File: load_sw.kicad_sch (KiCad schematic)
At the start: 49 parts, among them Q1 PSMN020-100YS, Q11 NMOS, Q16 NMOS, Q21 NMOS, Q22 NPN, Q23 NMOS, Q36 Q_NMOS, Q37 NPN, Q38 NMOS, Q6 NPN, U4 TPS16851VMAR, U5 LM5050-1

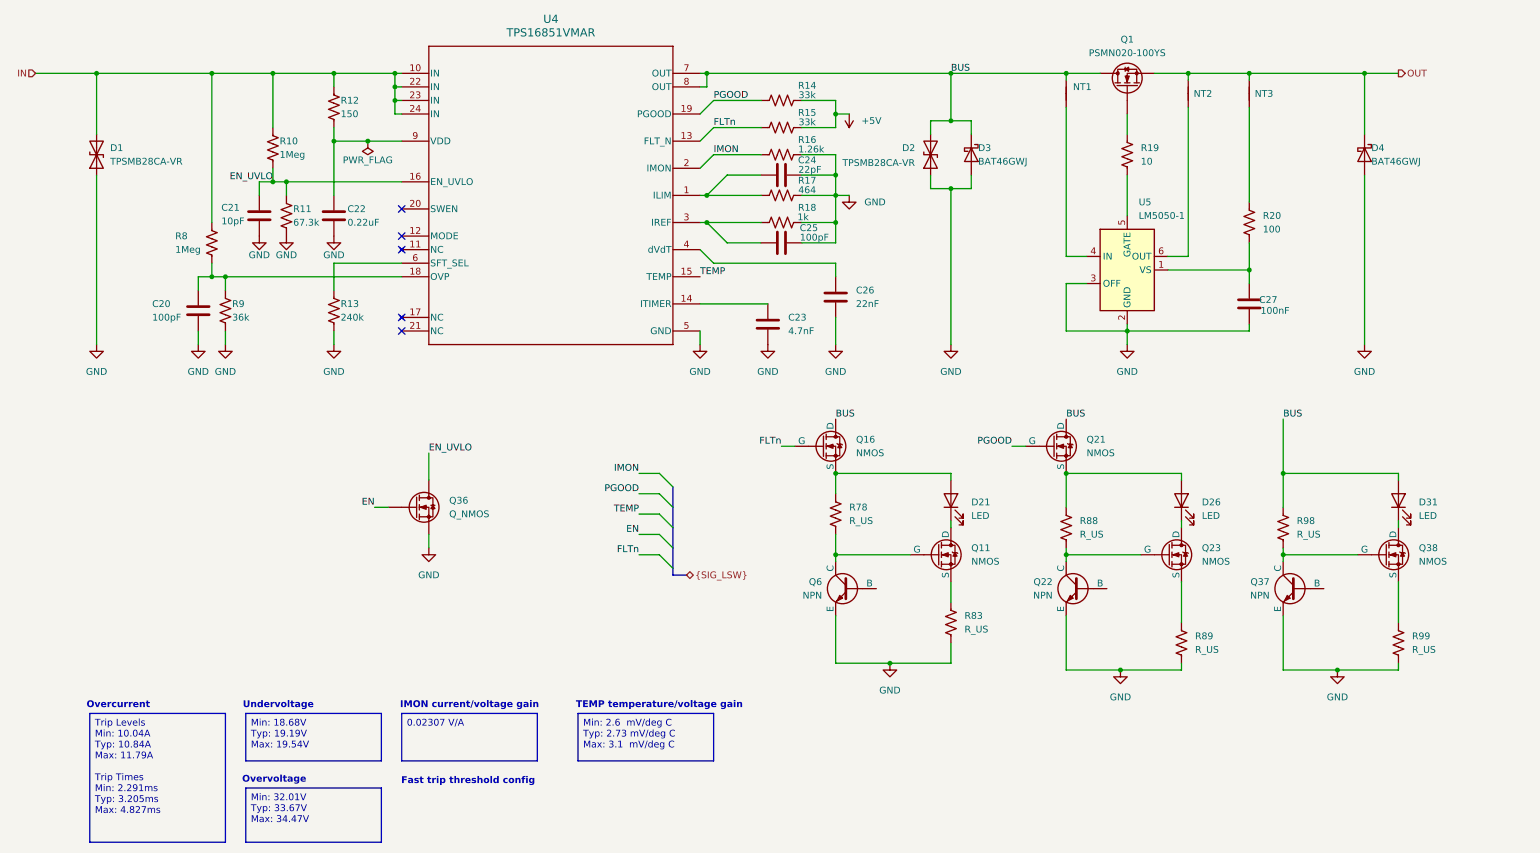
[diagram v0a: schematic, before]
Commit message: Finished layout for load switch dev board.
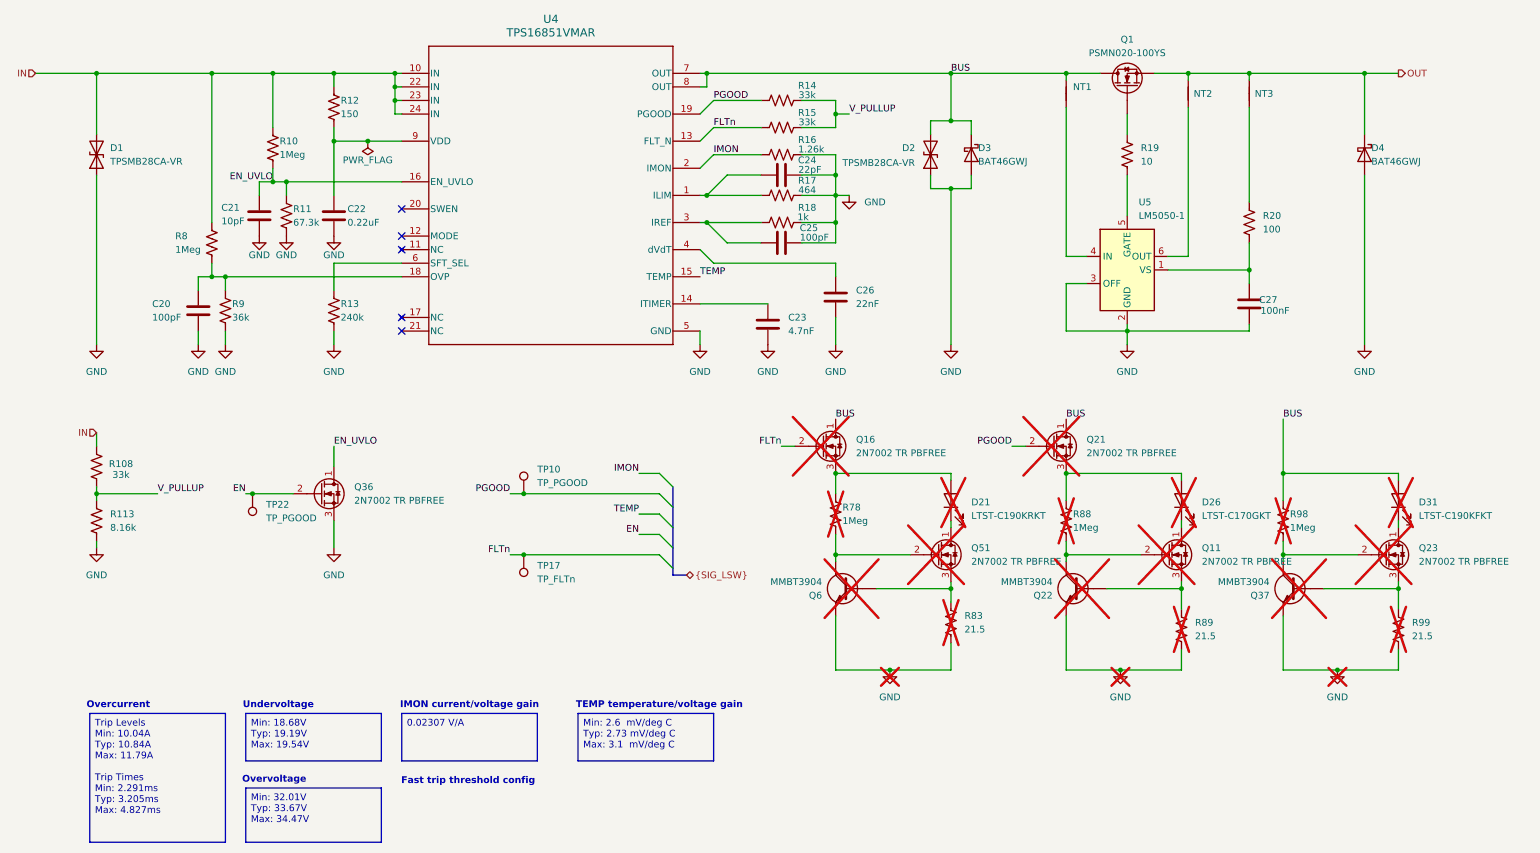
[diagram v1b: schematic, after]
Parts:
- removed Q11, Q16, Q21, Q23, Q38: NMOS, symbol Simulation_SPICE:NMOS
- removed Q22, Q37, Q6: NPN, symbol Simulation_SPICE:NPN
- removed Q36: Q_NMOS, symbol Device:Q_NMOS
- added Q11, Q16, Q21, Q23, Q36, Q51: 2N7002 TR PBFREE, Package_TO_SOT_SMD:TSOT-23, symbol Transistor_FET:Q_NMOS_DGS
- added Q22, Q37, Q6: MMBT3904, Package_TO_SOT_SMD:TSOT-23, symbol Device:Q_NPN
- added R108: 33k, Resistor_SMD:R_0603_1608Metric, symbol Device:R_US
- added R113: 8.16k, Resistor_SMD:R_0603_1608Metric, symbol Device:R_US
- added TP10, TP22: TP_PGOOD, TestPoint:TestPoint_Plated_Hole_D5.0mm, symbol Connector:TestPoint
- added TP17: TP_FLTn, TestPoint:TestPoint_Plated_Hole_D5.0mm, symbol Connector:TestPoint
- D21: value LED -> LTST-C190KRKT; footprint (none) -> LED_SMD:LED_0603_1608Metric; Mfr (none) -> Lite-On Inc.; Mfr P/N (none) -> LTST-C190KRKT; Supplier_1 (none) -> Digikey; Supplier_1 P/N (none) -> 160-1436-2-ND; Supplier_1 Price @ Qty (none) -> 1; Supplier_1 Unit Price (none) -> 0.14000; now not fitted; now left out of the parts list
- D26: value LED -> LTST-C170GKT; footprint (none) -> LED_SMD:LED_0805_2012Metric; Mfr (none) -> Lite-On Inc.; Mfr P/N (none) -> LTST-C170GKT; Supplier_1 (none) -> Digikey; Supplier_1 P/N (none) -> 160-1179-2-ND; Supplier_1 Price @ Qty (none) -> 1; Supplier_1 Unit Price (none) -> 0.10000; now not fitted; now left out of the parts list
- D31: value LED -> LTST-C190KFKT; footprint (none) -> LED_SMD:LED_0603_1608Metric; Mfr (none) -> Lite-On Inc.; Mfr P/N (none) -> LTST-C190KFKT; Supplier_1 (none) -> Digikey; Supplier_1 P/N (none) -> 160-1434-2-ND; Supplier_1 Price @ Qty (none) -> 1; Supplier_1 Unit Price (none) -> 0.13000; now not fitted; now left out of the parts list
- R78, R88, R98: value R_US -> 1Meg; footprint (none) -> Resistor_SMD:R_0603_1608Metric; Mfr (none) -> Stackpole Electronics Inc; Mfr P/N (none) -> RNCF0603BKC1M00; Supplier_1 (none) -> Digikey; Supplier_1 P/N (none) -> RNCF0603BKC1M00TR-ND; Supplier_1 Price @ Qty (none) -> 1; Supplier_1 Unit Price (none) -> 0.11000; now not fitted; now left out of the parts list
- R83, R89, R99: value R_US -> 21.5; footprint (none) -> Resistor_SMD:R_0603_1608Metric; Mfr (none) -> KOA Speer Electronics, Inc.; Mfr P/N (none) -> RN73R1JTTD21R5B25; Supplier_1 (none) -> Digikey; Supplier_1 P/N (none) -> 2019-RN73R1JTTD21R5B25TR-ND; Supplier_1 Price @ Qty (none) -> 0.12000; Supplier_1 Unit Price (none) -> 1; now not fitted; now left out of the parts list
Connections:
- net BUS: now also Q16.1 (D), Q21.1 (D)
- net EN: now also Q36.2 (G), TP22.1
- net EN_UVLO: now also Q36.1 (D)
- net FLTn: now also Q16.2 (G), TP17.1
- net GND: now also Q22.E, Q36.3 (S), Q37.E, Q6.E, R113.2
- net IN: now also R108.2
- net PGOOD: now also Q21.2 (G), TP10.1
- net at D31.1 (K): now also Q23.1 (D)
- net at R98.2: now also Q23.2 (G), Q37.C
- net at R99.1: now also Q23.3 (S), Q37.B
- net at R83.1: now also Q51.3 (S), Q6.B
- net at R88.2: now also Q11.2 (G), Q22.C
- net at D26.2 (A), R88.1: now also Q21.3 (S)
- net at R89.1: now also Q11.3 (S), Q22.B
- net at D21.2 (A), R78.1: now also Q16.3 (S)
- net at D21.1 (K): now also Q51.1 (D)
- net at R78.2: now also Q51.2 (G), Q6.C
- net at D26.1 (K): now also Q11.1 (D)
- net +5V renamed V_PULLUP
- net V_PULLUP: now also R108.1, R113.1

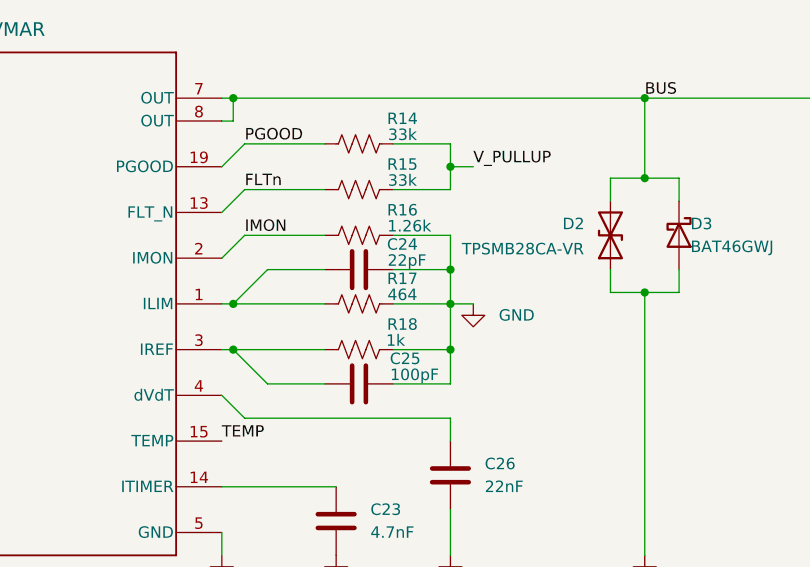
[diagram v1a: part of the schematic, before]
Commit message: Removing pads and adding more TPs and also mounting holes
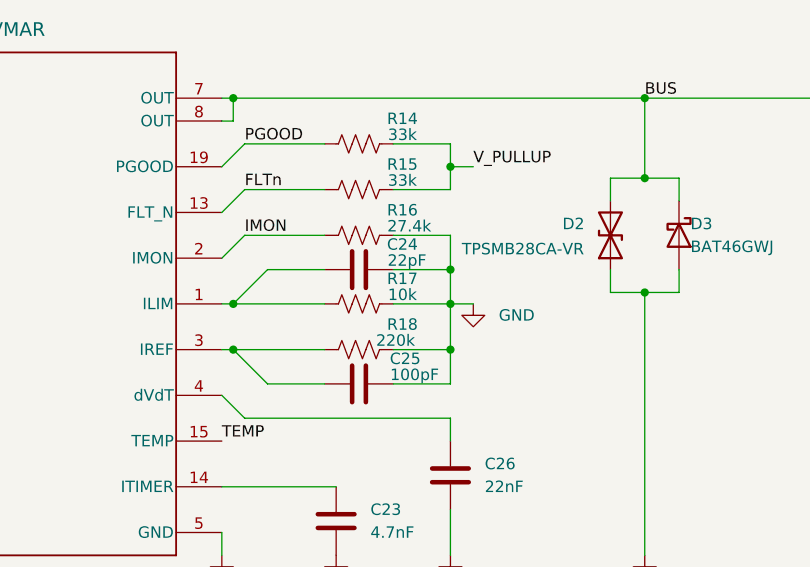
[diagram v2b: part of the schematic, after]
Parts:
- R16: value 1.26k -> 27.4k; Mfr KOA Speer Electronics, Inc. -> Panasonic Electronic Components; Mfr P/N RN73R1JTTD1261B25 -> ERA-3AEB2742V; Supplier_1 P/N 2019-RN73R1JTTD1261B25TR-ND -> P27.4KDBTR-ND; Supplier_1 Unit Price 0.12000 -> 0.10000
- R17: value 464 -> 10k; Mfr P/N ERA-3AEB4640V -> ERA-3AEB103V; Supplier_1 P/N 10-ERA-3AEB4640VTR-ND -> P10KDBTR-ND
- R18: value 1k -> 220k; Mfr P/N ERA-3AEB103V -> ERA-3AEB2742V; Supplier_1 P/N P10KDBTR-ND -> P27.4KDBTR-ND
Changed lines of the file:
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@@
 			)
 		)
-		(property "Value" "464"
+		(property "Value" "10k"
 			(at 164.846 53.594 90)
 			(effects
@@
 			)
 		)
-		(property "Description" "RES SMD 464 OHM 0.1% 1/10W 0603"
+		(property "Description" "RES SMD 10K OHM 0.1% 1/10W 0603"
 			(at 160.02 54.61 0)
 			(effects
@@
 			)
 		)
-		(property "Mfr P/N" "ERA-3AEB4640V"
+		(property "Mfr P/N" "ERA-3AEB103V"
 			(at 160.02 54.61 0)
 			(effects
@@
 			)
 		)
-		(property "Supplier_1 P/N" "10-ERA-3AEB4640VTR-ND"
+		(property "Supplier_1 P/N" "P10KDBTR-ND"
 			(at 160.02 54.61 0)
 			(effects
@@
 			)
 		)
-		(property "Value" "1.26k"
+		(property "Value" "27.4k"
 			(at 165.608 45.974 90)
 			(effects
@@
 			)
 		)
-		(property "Datasheet" "https://www.koaspeer.com/pdfs/RN73R.pdf"
+		(property "Datasheet" "https://industrial.panasonic.com/cdbs/www-data/pdf/RDM0000/AOA0000C307.pdf"
 			(at 160.02 46.99 0)
 			(effects
@@
 			)
 		)
-		(property "Description" "RES 1.26K OHM 0.1% 1/10W 0603"
+		(property "Description" "RES SMD 27.4KOHM 0.1% 1/10W 0603"
 			(at 160.02 46.99 0)
 			(effects
@@
 			)
 		)
-		(property "Mfr" "KOA Speer Electronics, Inc."
+		(property "Mfr" "Panasonic Electronic Components"
 			(at 160.02 46.99 0)
 			(effects
@@
 			)
 		)
-		(property "Mfr P/N" "RN73R1JTTD1261B25"
+		(property "Mfr P/N" "ERA-3AEB2742V"
 			(at 160.02 46.99 0)
 			(effects
@@
 			)
 		)
-		(property "Supplier_1 P/N" "2019-RN73R1JTTD1261B25TR-ND"
+		(property "Supplier_1 P/N" "P27.4KDBTR-ND"
 			(at 160.02 46.99 0)
 			(effects
@@
 			)
 		)
-		(property "Supplier_1 Unit Price" "0.12000"
+		(property "Supplier_1 Unit Price" "0.10000"
 			(at 160.02 46.99 0)
 			(effects
@@
 			)
 		)
-		(property "Value" "1k"
+		(property "Value" "220k"
 			(at 164.084 58.674 90)
 			(effects
@@
 			)
 		)
-		(property "Description" "RES SMD 10K OHM 0.1% 1/10W 0603"
+		(property "Description" "RES SMD 27.4KOHM 0.1% 1/10W 0603"
 			(at 160.02 59.69 0)
 			(effects
@@
 			)
 		)
-		(property "Mfr P/N" "ERA-3AEB103V"
+		(property "Mfr P/N" "ERA-3AEB2742V"
 			(at 160.02 59.69 0)
 			(effects
@@
 			)
 		)
-		(property "Supplier_1 P/N" "P10KDBTR-ND"
+		(property "Supplier_1 P/N" "P27.4KDBTR-ND"
 			(at 160.02 59.69 0)
 			(effects

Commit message: Finishing up layout
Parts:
- R16: value 27.4k -> 5.49k; Mfr P/N ERA-3AEB2742V -> ERA-3AEB5491V; Supplier_1 P/N P27.4KDBTR-ND -> P5.49KDBTR-ND
- R17: value 10k -> 2k; Mfr P/N ERA-3AEB103V -> ERA-3AEB202V; Supplier_1 P/N P10KDBTR-ND -> P2.0KDBTR-ND
- R18: value 220k -> 44.8k; Mfr Panasonic Electronic Components -> KOA Speer Electronics, Inc.; Mfr P/N ERA-3AEB2742V -> RN73R1JTTD4482B25; Supplier_1 P/N P27.4KDBTR-ND -> 2019-RN73R1JTTD4482B25TR-ND
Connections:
- net BUS: now also Q1.S; no longer Q1.D
- net OUT: now also Q1.D; no longer Q1.S
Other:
- moved on the sheet: Q1
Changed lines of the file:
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@@
 		)
 	)
-	(text_box "Trip Levels\nMin: 10.04A\nTyp: 10.84A\nMax: 11.79A\n\nTrip Times\nMin: 2.291ms\nTyp: 3.205ms\nMax: 4.827ms"
+	(text_box "Trip Levels\nMin: 10.32A\nTyp: 11.14A\nMax: 12.12A\n\nTrip Times\nMin: 2.291ms\nTyp: 3.205ms\nMax: 4.827ms"
 		(exclude_from_sim no)
 		(at 30.48 151.638 0)
@@
 		)
 	)
-	(text_box "0.02307 V/A"
+	(text_box "0.10052 V/A (nom)"
 		(exclude_from_sim no)
 		(at 88.9 151.638 0)
@@
 			)
 		)
-		(property "Value" "10k"
+		(property "Value" "2k"
 			(at 164.846 53.594 90)
 			(effects
@@
 			)
 		)
-		(property "Description" "RES SMD 10K OHM 0.1% 1/10W 0603"
+		(property "Description" "RES SMD 2K OHM 0.1% 1/10W 0603"
 			(at 160.02 54.61 0)
 			(effects
@@
 			)
 		)
-		(property "Mfr P/N" "ERA-3AEB103V"
+		(property "Mfr P/N" "ERA-3AEB202V"
 			(at 160.02 54.61 0)
 			(effects
@@
 			)
 		)
-		(property "Supplier_1 P/N" "P10KDBTR-ND"
+		(property "Supplier_1 P/N" "P2.0KDBTR-ND"
 			(at 160.02 54.61 0)
 			(effects
@@
 			)
 		)
-		(property "Value" "27.4k"
+		(property "Value" "5.49k"
 			(at 165.608 45.974 90)
 			(effects
@@
 			)
 		)
-		(property "Description" "RES SMD 27.4KOHM 0.1% 1/10W 0603"
+		(property "Description" "RES SMD 5.49KOHM 0.1% 1/10W 0603"
 			(at 160.02 46.99 0)
 			(effects
@@
 			)
 		)
-		(property "Mfr P/N" "ERA-3AEB2742V"
+		(property "Mfr P/N" "ERA-3AEB5491V"
 			(at 160.02 46.99 0)
 			(effects
@@
 			)
 		)
-		(property "Supplier_1 P/N" "P27.4KDBTR-ND"
+		(property "Supplier_1 P/N" "P5.49KDBTR-ND"
 			(at 160.02 46.99 0)
 			(effects
@@
 			)
 		)
-		(property "Value" "220k"
+		(property "Value" "44.8k"
 			(at 164.084 58.674 90)
 			(effects
@@
 			)
 		)
-		(property "Datasheet" "https://industrial.panasonic.com/cdbs/www-data/pdf/RDM0000/AOA0000C307.pdf"
+		(property "Datasheet" "https://www.koaspeer.com/pdfs/RN73R.pdf"
 			(at 160.02 59.69 0)
 			(effects
@@
 			)
 		)
-		(property "Description" "RES SMD 27.4KOHM 0.1% 1/10W 0603"
+		(property "Description" "RES 44.8K OHM 0.1% 1/10W 0603"
 			(at 160.02 59.69 0)
 			(effects
@@
 			)
 		)
-		(property "Mfr" "Panasonic Electronic Components"
+		(property "Mfr" "KOA Speer Electronics, Inc."
 			(at 160.02 59.69 0)
 			(effects
@@
 			)
 		)
-		(property "Mfr P/N" "ERA-3AEB2742V"
+		(property "Mfr P/N" "RN73R1JTTD4482B25"
 			(at 160.02 59.69 0)
 			(effects
@@
 			)
 		)
-		(property "Supplier_1 P/N" "P27.4KDBTR-ND"
+		(property "Supplier_1 P/N" "2019-RN73R1JTTD4482B25TR-ND"
 			(at 160.02 59.69 0)
 			(effects
@@
 	(symbol
 		(lib_id "Device:Q_NMOS")
-		(at 224.79 34.29 90)
+		(at 224.79 34.29 270)
+		(mirror x)
 		(unit 1)
 		(exclude_from_sim no)
@@
 		(on_board yes)
 		(dnp no)
-		(fields_autoplaced yes)
 		(property "Reference" "Q1"
 			(at 224.79 25.4 90)
@@
 		)
 		(property "Footprint" "_Power_Board:LFPAK56_1"
-			(at 222.25 29.21 0)
+			(at 227.33 29.21 0)
 			(effects
 				(font
@@
 			)
 		)
-		(property "Datasheet" "~"
+		(property "Datasheet" "https://my.centralsemi.com/datasheets/2N7002.PDF"
 			(at 73.66 110.49 0)
 			(effects

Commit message: Fixed cap values
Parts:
- C22: Mfr KEMET -> YAGEO; Mfr P/N C0603C221F5GACAUTO -> CC0603JRX7R9BB224; Supplier_1 P/N 399-C0603C221F5GACAUTOTR-ND -> 13-CC0603JRX7R9BB224TR-ND; Supplier_1 Unit Price 0.85000 -> 0.15000
- C23: Mfr P/N GCM1885C2A471FA16D -> GCM1885C1H472FA16D; Supplier_1 P/N 490-GCM1885C2A471FA16DTR-ND -> 490-GCM1885C1H472FA16DTR-ND; Supplier_1 Unit Price 0.16000 -> 0.18000
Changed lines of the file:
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@@
 			)
 		)
-		(property "Datasheet" "https://search.murata.co.jp/Ceramy/image/img/A01X/G101/ENG/GCM1885C2A471FA16-01.pdf"
+		(property "Datasheet" "https://search.murata.co.jp/Ceramy/image/img/A01X/G101/ENG/GCM1885C1H472FA16-01A.pdf"
 			(at 157.48 78.74 0)
 			(effects
@@
 			)
 		)
-		(property "Description" "CAP CER 470PF 100V C0G/NP0 0603"
+		(property "Description" "CAP CER 4700PF 50V C0G/NP0 0603"
 			(at 157.48 78.74 0)
 			(effects
@@
 			)
 		)
-		(property "Mfr P/N" "GCM1885C2A471FA16D"
+		(property "Mfr P/N" "GCM1885C1H472FA16D"
 			(at 157.48 78.74 0)
 			(effects
@@
 			)
 		)
-		(property "Supplier_1 P/N" "490-GCM1885C2A471FA16DTR-ND"
+		(property "Supplier_1 P/N" "490-GCM1885C1H472FA16DTR-ND"
 			(at 157.48 78.74 0)
 			(effects
@@
 			)
 		)
-		(property "Supplier_1 Unit Price" "0.16000"
+		(property "Supplier_1 Unit Price" "0.18000"
 			(at 157.48 78.74 0)
 			(effects
@@
 			)
 		)
-		(property "Datasheet" "https://search.kemet.com/download/datasheet/C0603C221F5GACAUTO"
+		(property "Datasheet" "https://www.yageogroup.com/content/datasheet/asset/file/UPY-GPHC_X7R_6_3V-TO-250V"
 			(at 76.2 58.42 0)
 			(effects
@@
 			)
 		)
-		(property "Description" "CAP CER 220PF 50V C0G/NP0 0603"
+		(property "Description" "CAP CER 0.22UF 50V X7R 0603"
 			(at 76.2 58.42 0)
 			(effects
@@
 			)
 		)
-		(property "Mfr" "KEMET"
+		(property "Mfr" "YAGEO"
 			(at 76.2 58.42 0)
 			(effects
@@
 			)
 		)
-		(property "Mfr P/N" "C0603C221F5GACAUTO"
+		(property "Mfr P/N" "CC0603JRX7R9BB224"
 			(at 76.2 58.42 0)
 			(effects
@@
 			)
 		)
-		(property "Supplier_1 P/N" "399-C0603C221F5GACAUTOTR-ND"
+		(property "Supplier_1 P/N" "13-CC0603JRX7R9BB224TR-ND"
 			(at 76.2 58.42 0)
 			(effects
@@
 			)
 		)
-		(property "Supplier_1 Unit Price" "0.85000"
+		(property "Supplier_1 Unit Price" "0.15000"
 			(at 76.2 58.42 0)
 			(effects
